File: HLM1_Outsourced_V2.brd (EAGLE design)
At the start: 101.6 x 88.9 mm, 33 parts, among them Q1 600mA/40V, Q2 MOSFET, Q3 MOSFET, SW1 SW1

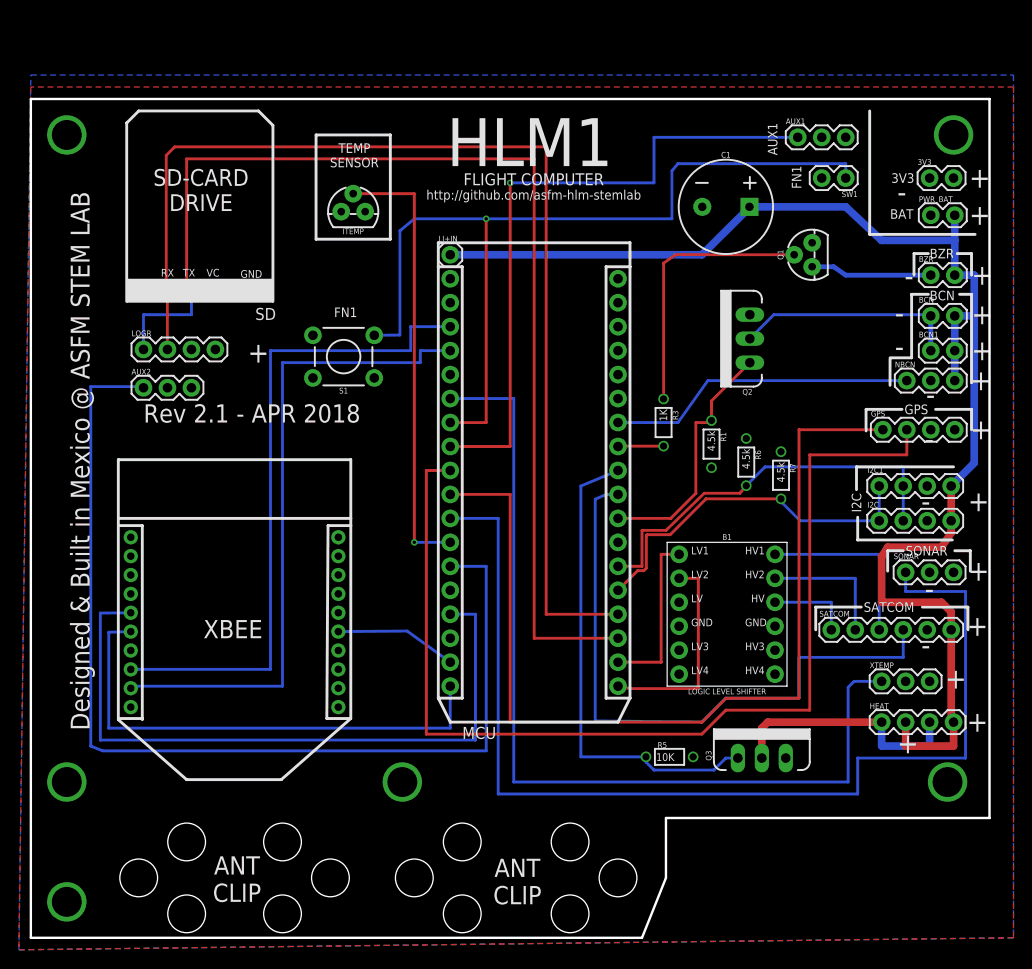
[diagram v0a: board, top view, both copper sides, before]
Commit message: Updated flight board to add XBee radio
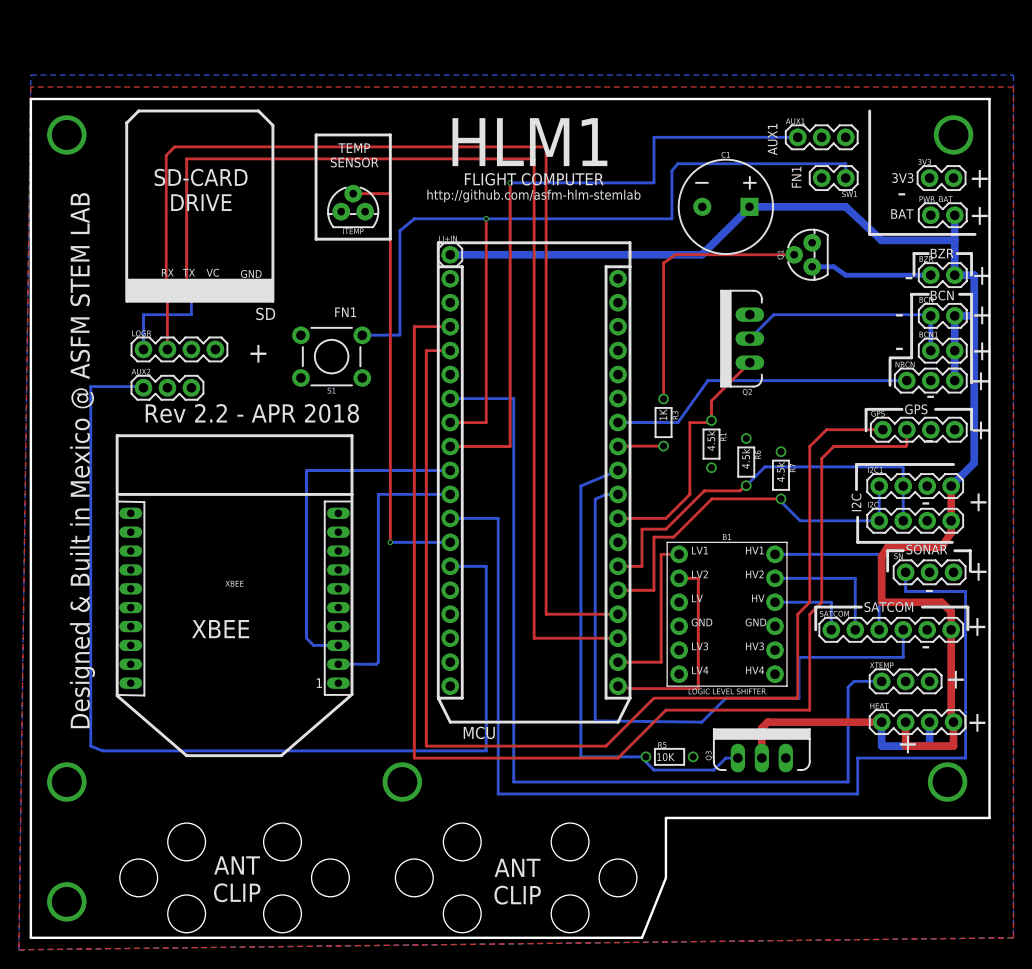
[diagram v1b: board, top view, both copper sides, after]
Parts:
- removed JP1: (no value), SparkFun-RF:XBEE
- added XBEE: RAD, SparkFun-RF:XBEE-LONGPAD
- moved S1 1.27 mm to (26.8, 62.9)
- renumbered SONAR to SN
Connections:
- removed net N$12: GPS.2, MCU.9
- removed net N$2: GPS.1, MCU.10
- removed net N$20: JP1.3, MCU.3
- removed net N$22: JP1.2, MCU.4
- removed net X_RESET: JP1.5, MCU.18
- removed net X_RSSI: JP1.6, MCU.15
- removed net X_RTS: JP1.16, MCU.17
- new net GPSRX: GPS.1, MCU.4
- new net GPSTX: GPS.2, MCU.3
- new net XBEE_DIN: MCU.9, XBEE.3
- new net XBEE_DOUT: MCU.10, XBEE.2
- net 3.3V: now also XBEE.1; no longer JP1.1
- net GND: now also XBEE.10; no longer JP1.10
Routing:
- net GPSTX: track 0.00 -> 132.0 mm
- net GPSRX: track 0.00 -> 121.6 mm
- net N$12: track 112.2 -> 0.00 mm
- net N$2: track 99.5 -> 0.00 mm
- net X_RSSI: track 72.4 -> 0.00 mm
- net N$22: track 70.3 -> 0.00 mm
- net N$20: track 70.2 -> 0.00 mm
- net X_RESET: track 53.1 -> 0.00 mm
- net XBEE_DIN: track 0.00 -> 36.7 mm
- net XBEE_DOUT: track 0.00 -> 29.7 mm
- net X_RTS: track 12.9 -> 0.00 mm
- net SCL: track 38.5 -> 39.8 mm
- net N$15: track 93.8 -> 95.1 mm
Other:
- board text added: "ASFM | HLM 1 | V2.2"
- board text added: "Rev 2.2 - APR 2018"
- board text removed: "ASFM | HLM 1 | V2.1"
- board text removed: "Rev 2.1 - APR 2018"
